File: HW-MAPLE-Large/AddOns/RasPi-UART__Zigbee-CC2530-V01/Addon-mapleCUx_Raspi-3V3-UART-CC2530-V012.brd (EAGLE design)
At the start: 49 x 47 mm, 21 parts, among them IC1 LD117ADT50TR, IC6 LM1117MPX-ADJ, X4 1751248

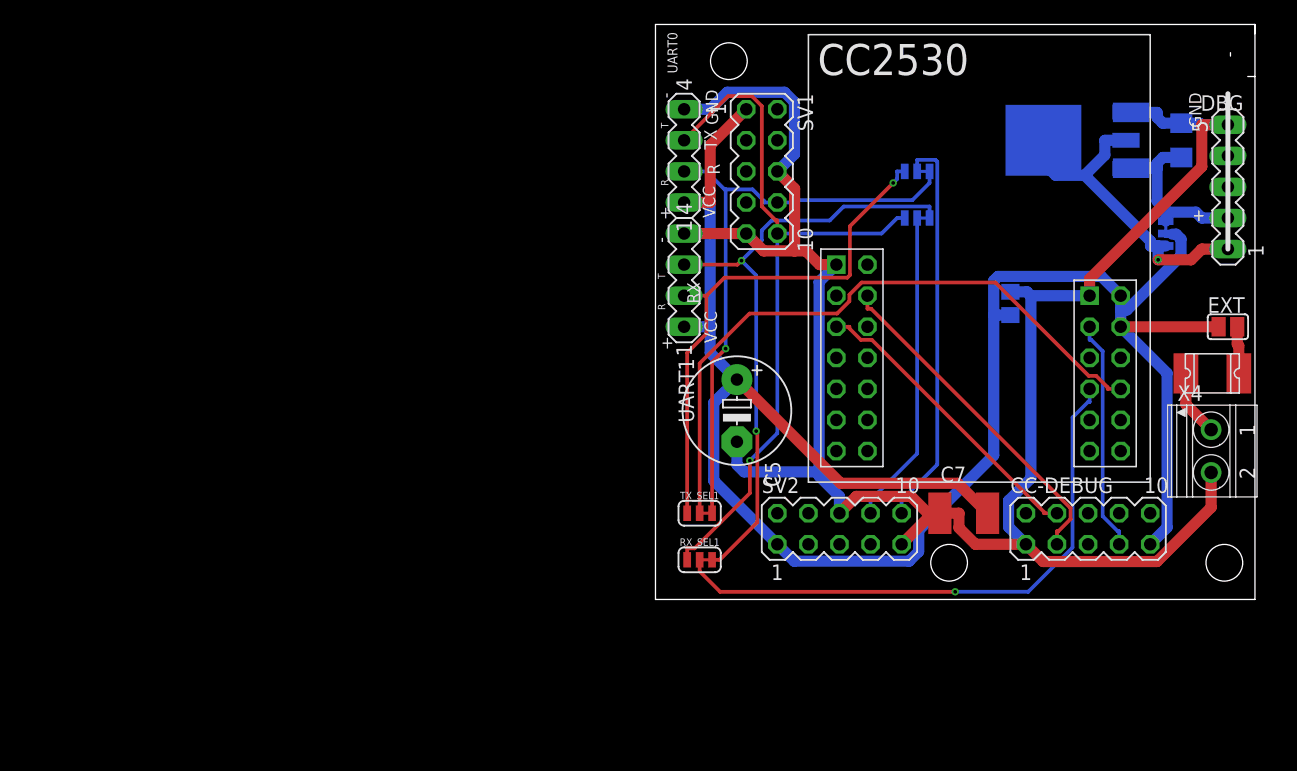
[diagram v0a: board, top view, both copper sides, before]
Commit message: Case from Thingiverse; Zigbee/RaspiAddOn
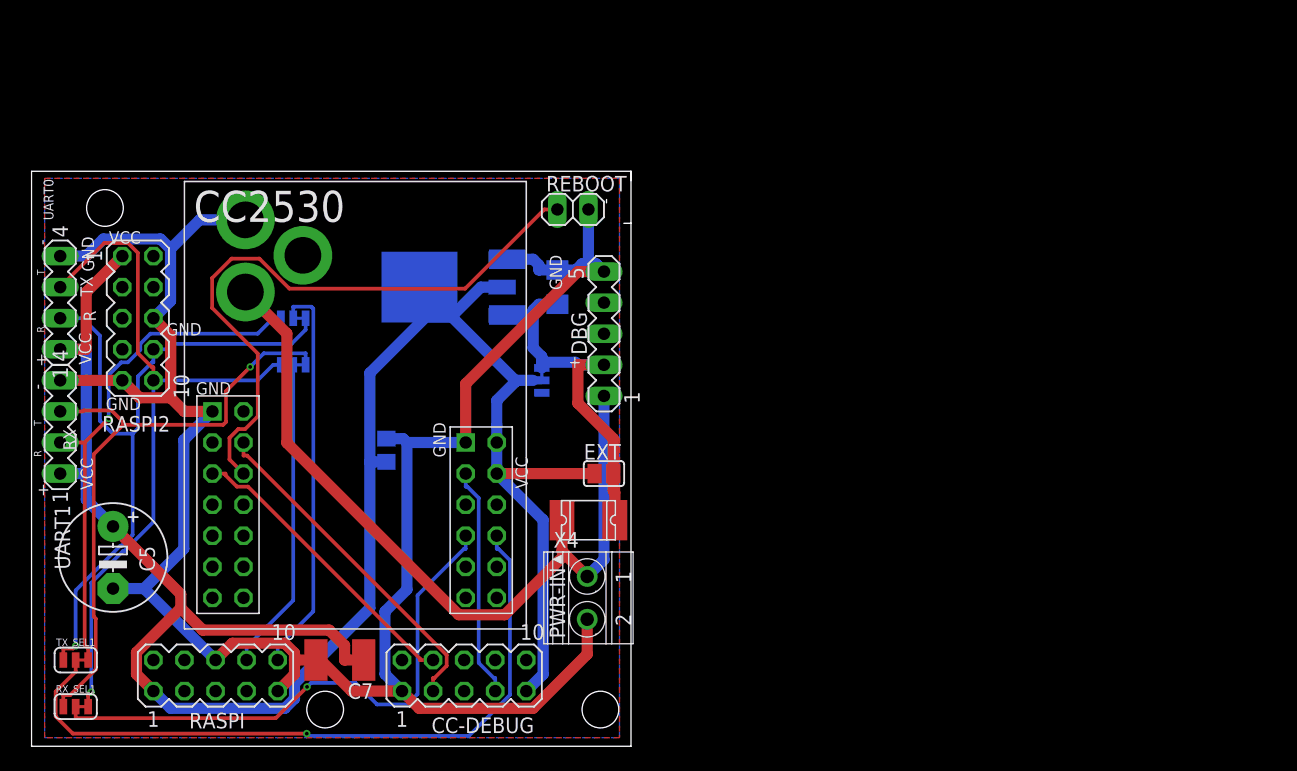
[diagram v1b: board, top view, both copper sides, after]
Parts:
- removed SV1, SV2: (no value), con-lstb:MA05-2
- added RASPI, RASPI2: (no value), con-lstb:MA05-2
- added REBOOT: (no value), pinhead:1X02
- added U$2: 2.1MMJACKTHM, adafruit:PJ-102A
- moved C9 52.4 mm to (43.0, 37.5)
- moved DBG 52.4 mm to (46.8, 33.7)
- moved EXT 52.4 mm to (46.8, 22.3)
- moved C5 52.4 mm to (6.66, 15.4)
- moved C6 52.4 mm to (29.0, 24.2)
- moved C7 52.4 mm to (25.2, 7.05)
- moved CC-DEBUG 52.4 mm to (35.4, 5.78)
- moved IC1 52.4 mm to (34.1, 37.5)
- moved IC6 52.4 mm to (35.4, 37.5)
- moved RX_SEL 52.4 mm to (21.4, 31.2)
- moved RX_SEL1 52.4 mm to (3.61, 3.24)
- moved TX_SEL 52.4 mm to (21.4, 35.0)
- moved TX_SEL1 52.4 mm to (3.61, 7.05)
- moved U$3 52.4 mm to (26.5, 28.6)
- moved UART0 52.4 mm to (2.34, 36.3)
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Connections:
- removed net EXT: EXT.2, F1.P$1
- removed net N$45: F1.P$2, X4.1
- new net IN2: DBG.1, F1.P$2, U$2.TIP, X4.1
- new net N$1: REBOOT.2, U$3.P2_0
- net GND: now also RASPI.6, RASPI.9, RASPI2.6, RASPI2.9, REBOOT.1, U$2.RING; no longer SV1.6, SV1.9, SV2.6, SV2.9
- net IN: now also EXT.2, F1.P$1
- net RX: now also RASPI.10; no longer SV2.10
- net RX0: now also RASPI2.10, RX_SEL1.3; no longer RX_SEL1.1, SV1.10
- net RX1: now also RX_SEL1.1; no longer RX_SEL1.3
- net TX: now also RASPI.8; no longer SV2.8
- net TX0: now also RASPI2.8, TX_SEL1.1; no longer SV1.8, TX_SEL1.3
- net TX1: now also TX_SEL1.3; no longer TX_SEL1.1
- net VCC: now also IC1.4, IC6.2, IC6.TAB, RASPI.1, RASPI2.1; no longer SV1.1, SV2.1
- net VIN2: no longer DBG.1, IC1.4, IC6.2, IC6.TAB
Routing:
- net IN2: track 0.00 -> 65.1 mm
- net N$1: track 0.00 -> 51.9 mm
- net VIN2: track 27.7 -> 0.00 mm, vias 1 -> 0
- net IN: track 15.0 -> 31.0 mm
- net VCC: track 161.7 -> 171.2 mm
- net GND: track 166.3 -> 174.8 mm
- net TX0: track 49.7 -> 57.0 mm
- net N$45: track 5.45 -> 0.00 mm
- net N$3: track 53.4 -> 58.0 mm, vias 0 -> 1
- net EXT: track 3.86 -> 0.00 mm
- net N$2: track 47.2 -> 45.8 mm
- net RX0: track 60.2 -> 59.1 mm
- net TX1: track 43.4 -> 42.5 mm
- net RX1: track 50.3 -> 51.1 mm, vias 2 -> 1
- added copper zone on layer 1, net GND
- added copper zone on layer 16, net GND
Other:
- board text added: "MAPLE-Cul AddOn"
- board text added: "PWR-IN"
- board text added: "VIN"
- board text added: "for 3V3 Serial Raspi AddOns and CC2530 V0.1"
- board text removed: "MAPLE-Cul AddOn for 3V3 Serial Raspi AddOns V0.1"
